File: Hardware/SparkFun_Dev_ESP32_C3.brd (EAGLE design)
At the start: 17.8 x 33 mm, 36 parts, among them J1 USB Female Type C Connector, J4 QWIIC_RIGHT_ANGLE, U1 ESP32-C3, U2 RT9080-33GJ5, U3 WS2812-2020, Y1 40MHZ

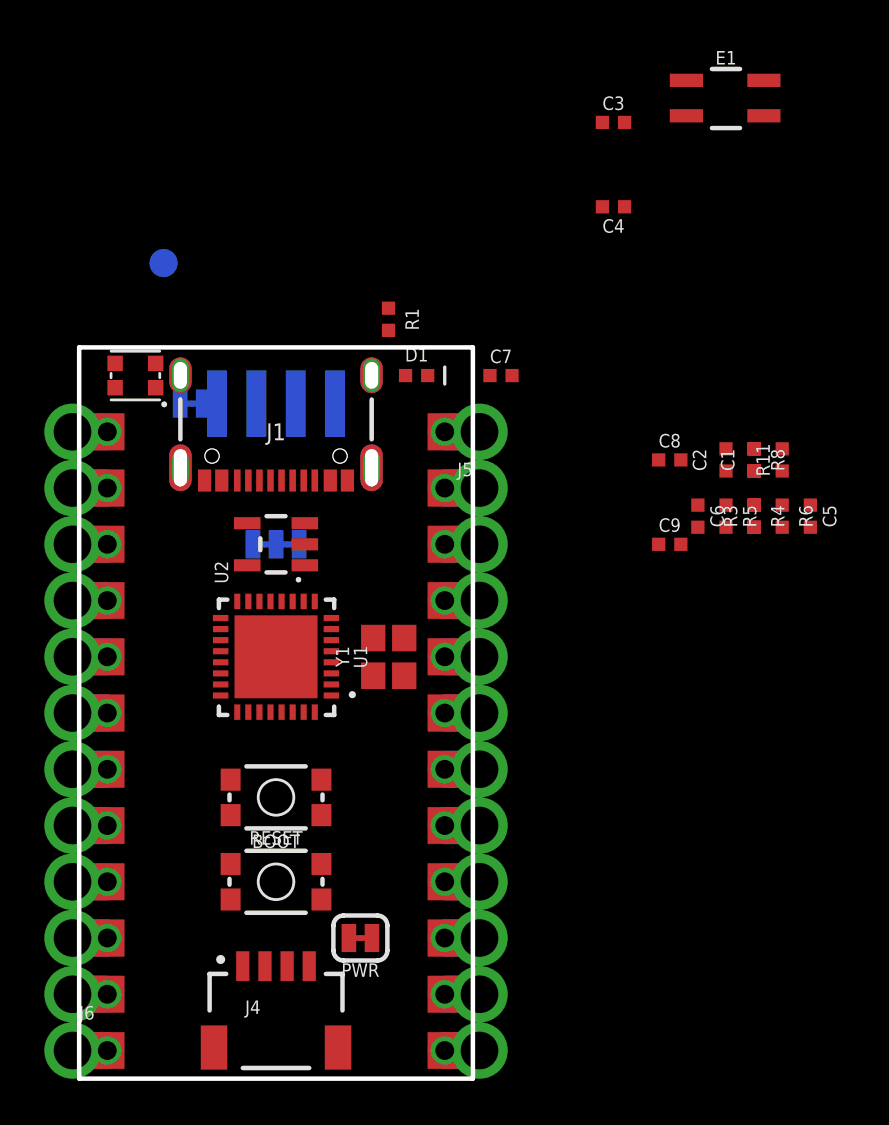
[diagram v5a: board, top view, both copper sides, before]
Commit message: Moves the parts into position
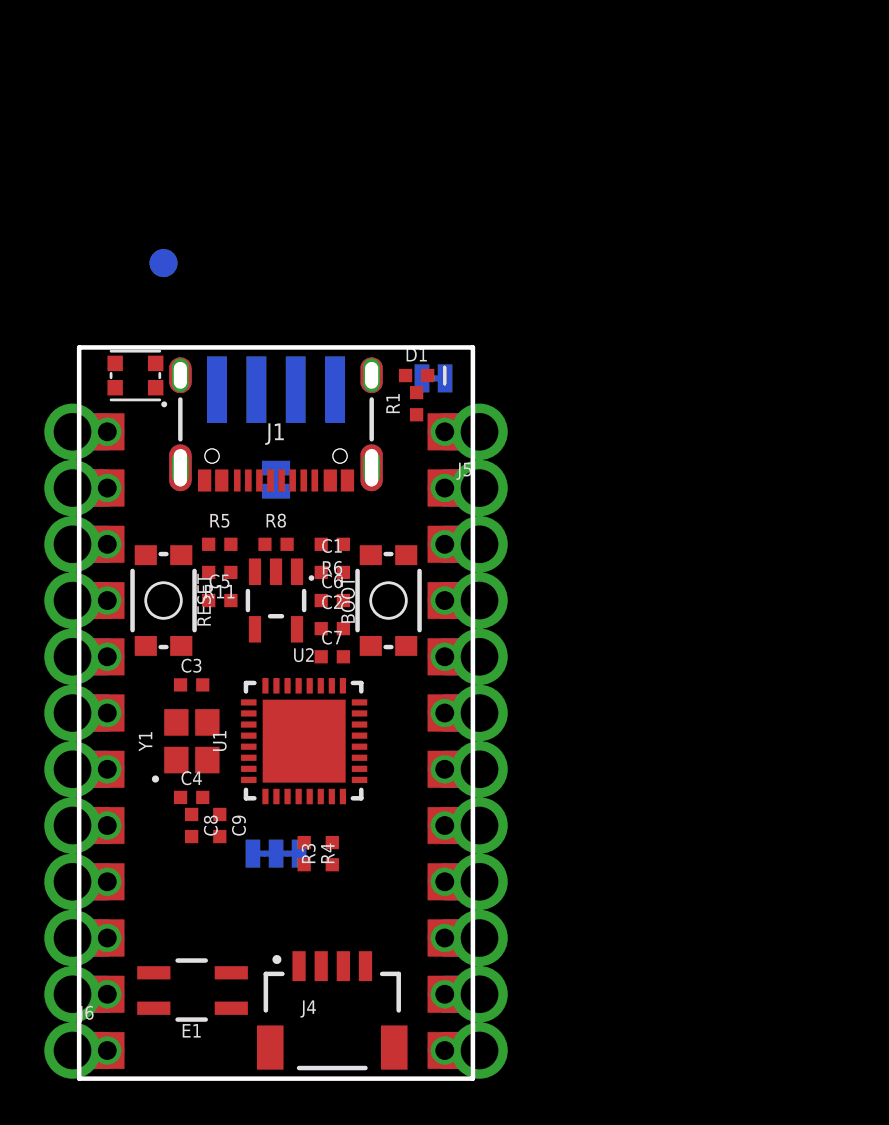
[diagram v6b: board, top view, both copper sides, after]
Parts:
- moved E1 47.3 mm to (6.35, 3.81), turned to 180 degrees
- moved C4 32.8 mm to (6.35, 12.7), turned to 0 degrees
- moved C3 31.8 mm to (6.35, 17.8)
- moved C8 27.2 mm to (6.35, 11.4), turned to 270 degrees
- moved C5 26.9 mm to (7.62, 21.6), turned to 0 degrees
- moved R11 25.9 mm to (7.62, 22.9), turned to 180 degrees
- moved PWR 25.5 mm to (17.3, 31.6), flipped to the bottom, turned to 0 degrees
- moved R4 25.4 mm to (11.4, 10.2)
- moved R3 24.4 mm to (12.7, 10.2)
- moved C9 24.0 mm to (7.62, 11.4), turned to 270 degrees
- moved R5 22.9 mm to (7.62, 24.1), turned to 0 degrees
- moved R8 21.9 mm to (10.2, 24.1), turned to 0 degrees
- moved R6 20.4 mm to (12.7, 24.1), turned to 180 degrees
- moved C1 19.7 mm to (12.7, 22.9), turned to 0 degrees
- moved C2 19.3 mm to (12.7, 20.3), turned to 0 degrees
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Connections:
- removed net IO9/BOOT: BOOT.3, BOOT.4, C6.1
- removed net N$11: E1.P1, U1.P1
- new net ANT: E1.P1
- new net IO8/BOOT: BOOT.3, BOOT.4, C6.1, U1.P14

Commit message: Fixes schematic
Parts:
- moved R4 2.84 mm to (12.7, 7.62), turned to 0 degrees
- moved C9 1.27 mm to (6.35, 11.4), turned to 180 degrees
- moved R3 1.27 mm to (12.7, 8.89), turned to 180 degrees
- moved C8 0.89 mm to (6.35, 12.3), turned to 180 degrees
- moved C4 0.51 mm to (6.35, 13.2)
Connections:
- removed net GND1: JP14.GND
- removed net RP_D+: JP14.D+
- removed net RP_D-: JP14.D-
- net GND: now also JP14.GND
- net IO18/USB_N: now also JP14.D-
- net IO19/USB_P: now also JP14.D+
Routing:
- removed copper zone on layer 15, net GND
- removed copper zone on layer 2, net GND
- removed copper zone on layer 15, net SHLD

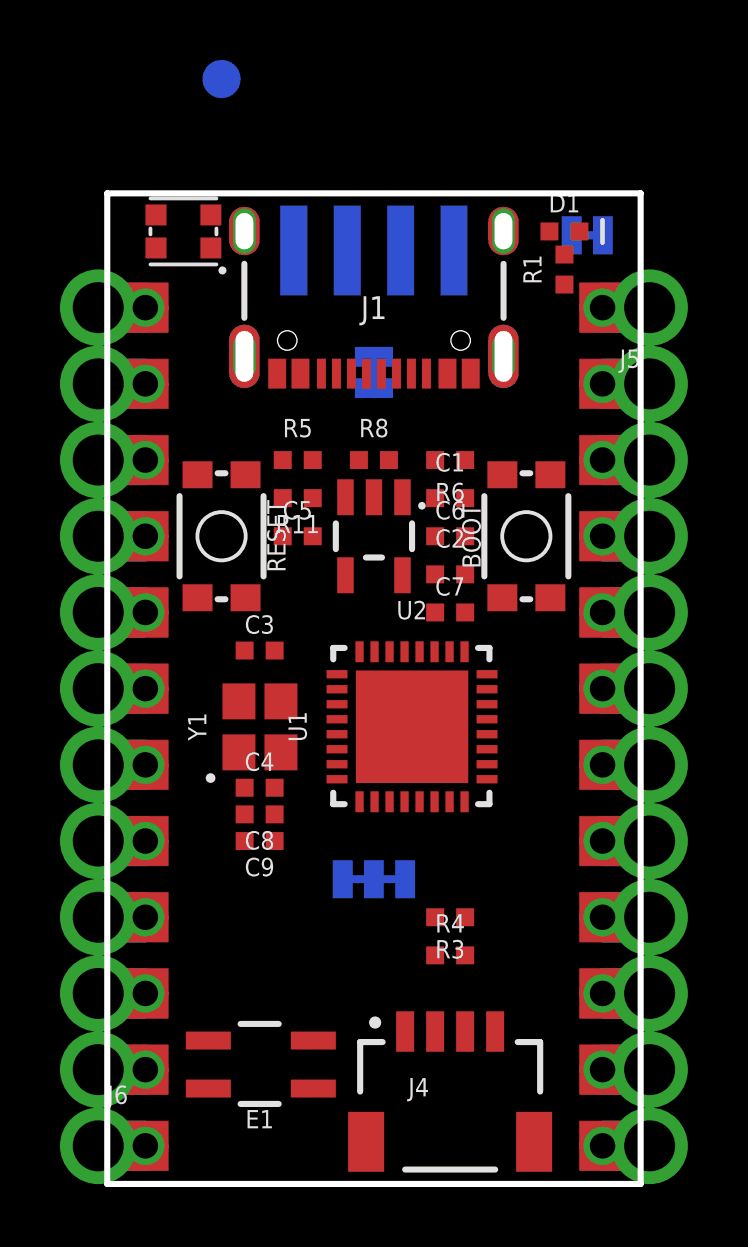
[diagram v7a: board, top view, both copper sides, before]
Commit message: More I/O netting from ESP32C3 to headers
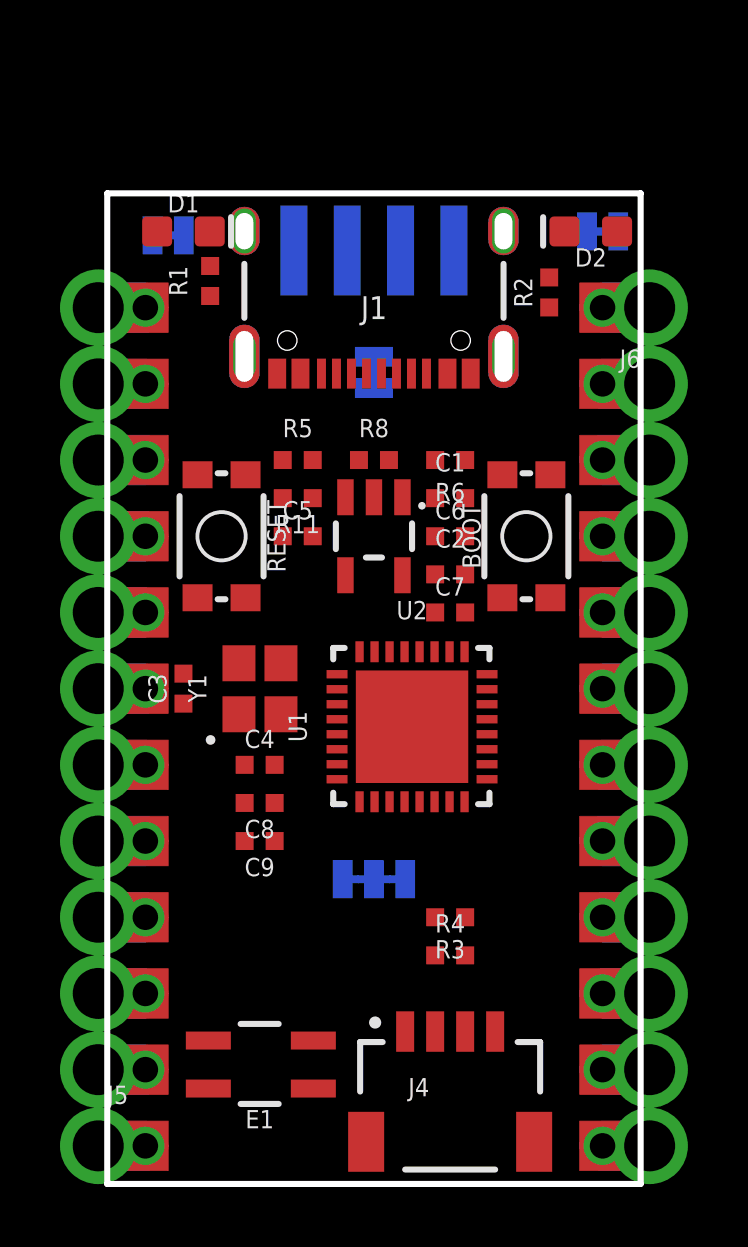
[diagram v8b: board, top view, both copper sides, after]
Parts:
- removed TP3: (no value), SparkFun-Connectors:PAD.03X.05
- removed U3: WS2812-2020, SparkFun-LED:WS2812-2020
- added D2: BLUE, SparkFun-LED:LED-0603
- added R2: 1k, SparkFun-Resistors:0402-TIGHT
- added STAT: JUMPER-SMT_2_NC_TRACE_SILK, SparkFun-Jumpers:SMT-JUMPER_2_NC_TRACE_SILK
- D1: device SparkFun-LED:LED-0402 -> SparkFun-LED:LED-0603
- moved FRAME2 53.4 mm to (-11.4, -25.4)
- moved J5 31.8 mm to (2.54, 1.27), turned to 0 degrees
- moved J6 31.8 mm to (17.8, 29.2), turned to 180 degrees
- moved PWR 14.0 mm to (3.30, 31.6)
- moved D1 12.7 mm to (3.81, 31.8)
- moved R1 11.8 mm to (4.70, 30.1)
- moved C3 2.84 mm to (3.81, 16.5), turned to 90 degrees
- moved Y1 1.27 mm to (6.35, 16.5)
- moved C4 0.76 mm to (6.35, 14.0)
- moved C8 0.38 mm to (6.35, 12.7)
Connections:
- removed net 0/TX0: J5.12, J5.12B
- removed net 1/RX0: J5.11, J5.11B
- removed net 2: J5.8, J5.8B
- removed net 20/SPI_CIPO: J6.10, J6.10B
- removed net 21/SPI_!CS!: J6.12, J6.12B
- removed net 22/SPI_SCK: J6.9, J6.9B
- removed net 23/SPI_COPI: J6.11, J6.11B
- removed net 25/WS2812-DI: U3.3
- removed net 3: J5.7, J5.7B
- removed net 4: J5.6, J5.6B
- removed net 5: J5.5, J5.5B
- removed net 6: J5.4, J5.4B
- removed net 7: J5.3, J5.3B
- removed net 8/TX1: J5.2, J5.2B
- removed net 9/RX1: J5.1, J5.1B
- removed net A0: J6.8, J6.8B
- removed net A1: J6.7, J6.7B
- removed net A2: J6.6, J6.6B
- removed net A3: J6.5, J6.5B
- removed net IO3: U1.P8
- removed net IO5: U1.P10
- removed net PICO: U1.P13
- removed net POCI: U1.P6
- removed net SCLK: U1.P12
- new net IO0/A0: J6.8, J6.8B, U1.P4
- new net IO1/A1: J6.7, J6.7B, U1.P5
- new net IO10: J5.8, J5.8B, U1.P16
- new net IO12: J5.7, J5.7B, U1.P19
- new net IO16: J5.5, J5.5B, U1.P23
- new net IO17: U1.P24
- new net IO2/POCI: J6.10, J6.10B, U1.P6
- new net IO3/A3: J6.5, J6.5B, U1.P8
- new net IO4/A4: U1.P9
- new net IO5/A5: J6.6, J6.6B, U1.P10
- new net IO6/SCLK: J6.9, J6.9B, U1.P12
- new net IO7/PICO: J6.11, J6.11B, U1.P13
- new net N$11: D2.A, STAT.1
- net 3.3V: now also STAT.2
- net ANT: now also U1.P1
- net GND: now also R2.1; no longer U3.2
- net IO13/SDA: now also J5.2, J5.2B
- net IO14/SCL: now also J5.1, J5.1B
- net IO15: now also J5.6, J5.6B
- net IO20/TX: now also J5.12, J5.12B
- net IO21/RX: now also J5.11, J5.11B
- net N$3: now also D2.C, R2.2; no longer TP3.P$1, U3.1
- net RAW: no longer U3.4
